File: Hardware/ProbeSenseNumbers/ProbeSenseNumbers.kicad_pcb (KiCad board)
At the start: 2 copper layers, 80.8 x 50.8 mm, 72 parts, among them J3 TopIn, J31 + - top, J32 + - bottom, J34 TopOut, J35 BottomIn, J4 BottomOut

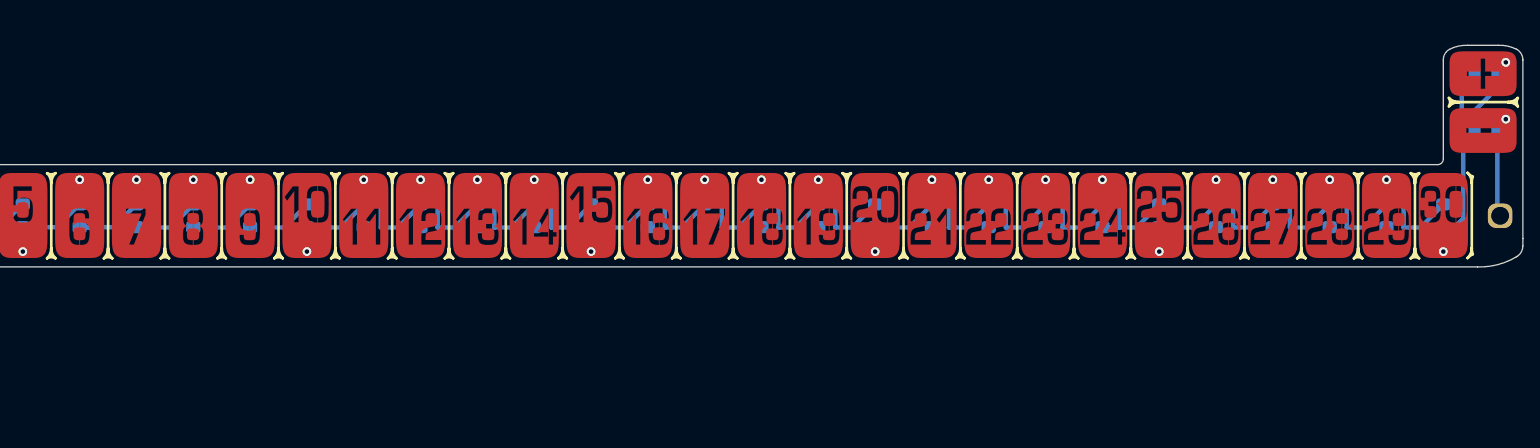
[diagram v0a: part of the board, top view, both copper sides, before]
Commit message: I'm dumb and forgot to route some tracks on the probe sense board
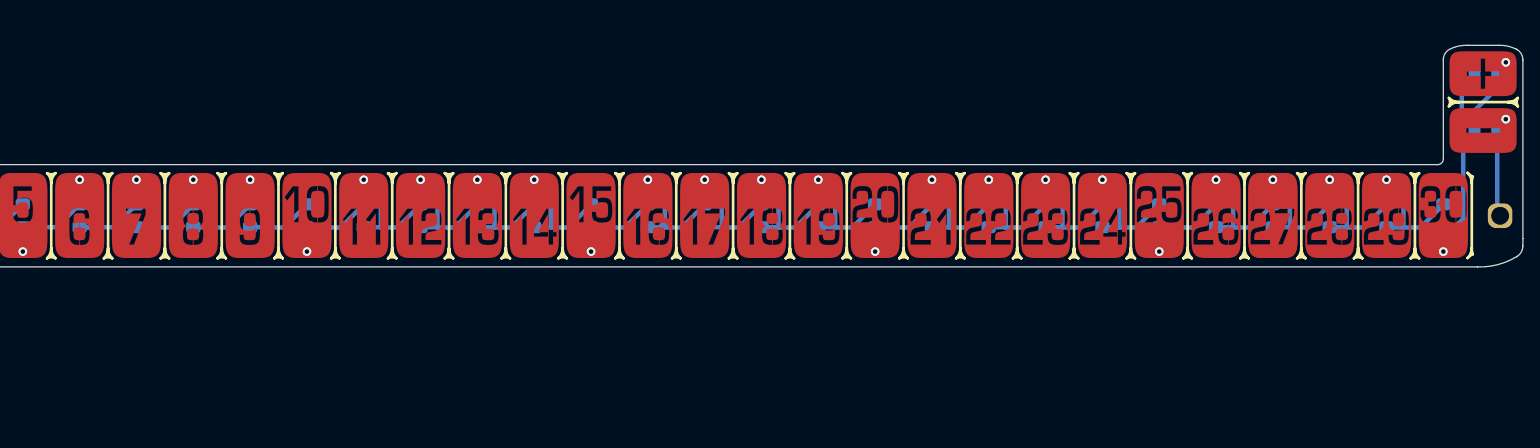
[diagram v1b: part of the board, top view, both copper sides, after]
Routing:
- net Net-(U1-Pin_16): track 4.65 -> 5.51 mm
- net Net-(U1-Pin_9): track 4.65 -> 5.42 mm
- net Net-(U1-Pin_23): track 4.65 -> 5.42 mm
- net Net-(U1-Pin_22): track 4.65 -> 5.42 mm
- net Net-(U1-Pin_18): track 4.65 -> 5.42 mm
- net Net-(U1-Pin_11): track 4.65 -> 5.42 mm
- net Net-(U1-Pin_8): track 4.65 -> 5.42 mm
- net Net-(U1-Pin_26): track 4.65 -> 5.42 mm
- net Net-(U1-Pin_19): track 4.65 -> 5.42 mm
- net Net-(U1-Pin_12): track 4.65 -> 5.42 mm
- net Net-(U1-Pin_7): track 4.65 -> 5.42 mm
- net Net-(U1-Pin_29): track 4.65 -> 5.42 mm
- net Net-(U1-Pin_28): track 4.65 -> 5.42 mm
- net Net-(U1-Pin_27): track 4.65 -> 5.42 mm
- net Net-(U1-Pin_21): track 4.65 -> 5.42 mm
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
